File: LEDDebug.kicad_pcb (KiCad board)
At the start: 2 copper layers, 17.5 x 23.9 mm, 34 parts, among them J1 Conn_01x09_Pin

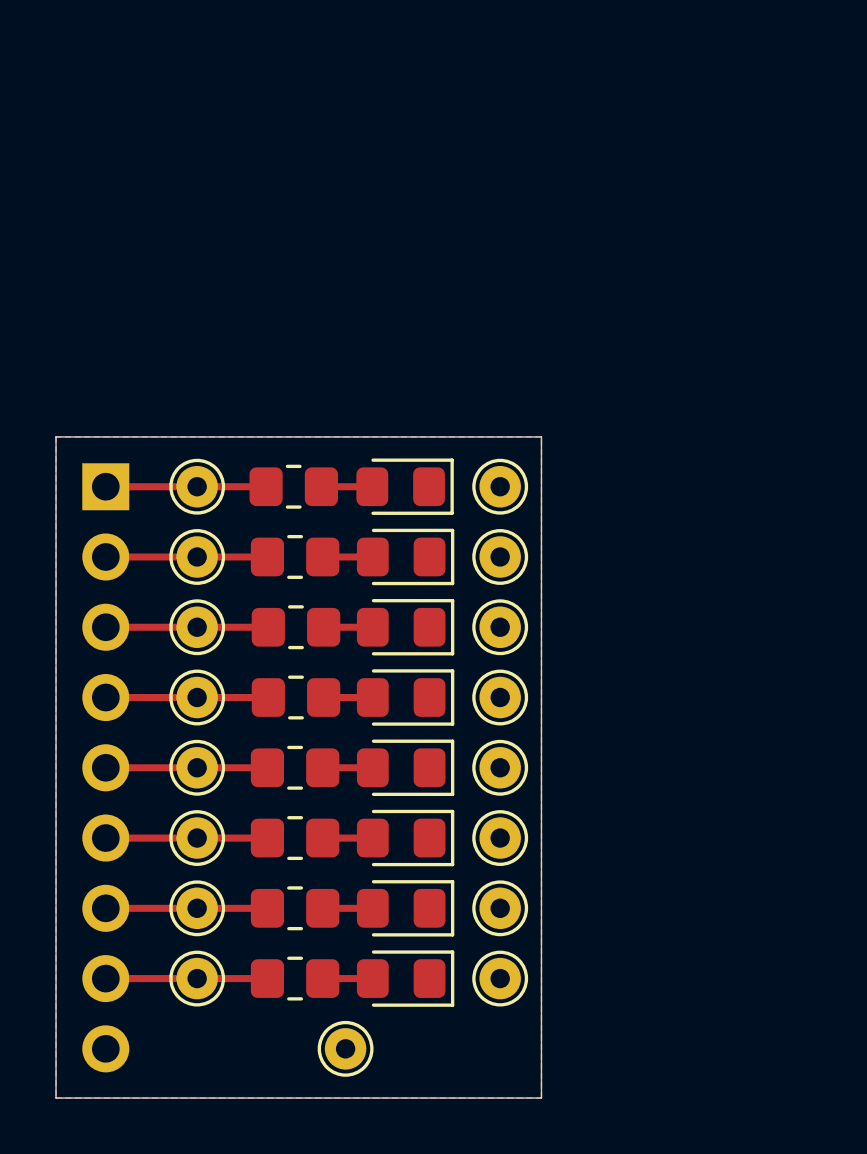
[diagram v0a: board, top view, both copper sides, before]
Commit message: Component sizing and placement update
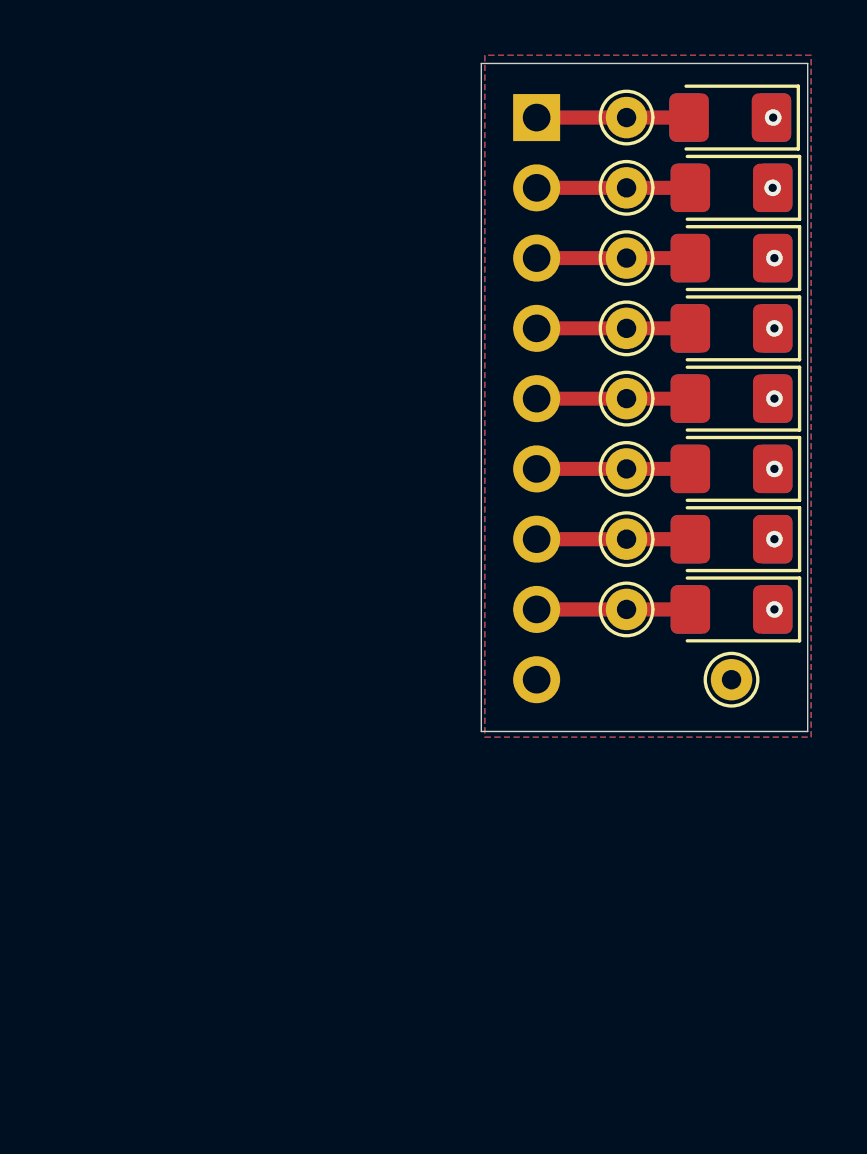
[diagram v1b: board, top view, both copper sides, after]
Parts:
- removed the GND1 at (57.2, 53.6)
- removed GND2, GND3, GND4, GND5, GND6, GND7, GND8: TestPoint, TestPoint:TestPoint_THTPad_D1.5mm_Drill0.7mm
- D1, D2, D3, D4, D5, D6, D7, D8: footprint LED_SMD:LED_0805_2012Metric_Pad1.15x1.40mm_HandSolder -> LED_SMD:LED_1206_3216Metric_Pad1.42x1.75mm_HandSolder
- R1, R2, R3, R4, R5, R6, R7, R8: footprint Resistor_SMD:R_0805_2012Metric_Pad1.20x1.40mm_HandSolder -> Resistor_SMD:R_1206_3216Metric_Pad1.30x1.75mm_HandSolder; moved to B.Cu
- moved R1 20.7 mm to (65.5, 40.2), turned to 0 degrees
- moved R2 20.7 mm to (65.5, 42.8), turned to 0 degrees
- moved R5 20.7 mm to (65.5, 50.4), turned to 0 degrees
- moved R7 20.7 mm to (65.5, 55.5), turned to 0 degrees
- moved R6 20.7 mm to (65.5, 53.0), turned to 0 degrees
- moved R8 20.7 mm to (65.5, 58.0), turned to 0 degrees
- moved R3 20.6 mm to (65.5, 45.3), turned to 0 degrees
- moved R4 20.6 mm to (65.5, 47.9), turned to 0 degrees
- moved J1 20.5 mm to (58.5, 40.2)
- moved TP1 20.5 mm to (61.8, 40.2)
- moved TP2 20.5 mm to (61.8, 42.8)
- moved TP3 20.5 mm to (61.8, 45.3)
- moved TP4 20.5 mm to (61.8, 47.9)
- moved TP5 20.5 mm to (61.8, 50.4)
- moved TP7 20.5 mm to (61.8, 55.5)
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- renumbered GND0 to GND1
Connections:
- D1 pad 1: GND -> Net-(D1-K)
- D1 pad 2: Net-(D1-A) -> TP1
- D2 pad 1: GND -> Net-(D2-K)
- D2 pad 2: Net-(D2-A) -> TP2
- D3 pad 1: GND -> Net-(D3-K)
- D3 pad 2: Net-(D3-A) -> TP3
- D4 pad 1: GND -> Net-(D4-K)
- D4 pad 2: Net-(D4-A) -> TP4
- D5 pad 1: GND -> Net-(D5-K)
- D5 pad 2: Net-(D5-A) -> TP5
- D6 pad 1: GND -> Net-(D6-K)
- D6 pad 2: Net-(D6-A) -> TP6
- D7 pad 1: GND -> Net-(D7-K)
- D7 pad 2: Net-(D7-A) -> TP7
- D8 pad 1: GND -> Net-(D8-K)
- D8 pad 2: Net-(D8-A) -> TP8
- R1 pad 1: Net-(D1-A) -> GND
- R1 pad 2: TP1 -> Net-(D1-K)
- R2 pad 1: Net-(D2-A) -> GND
- R2 pad 2: TP2 -> Net-(D2-K)
- R3 pad 1: Net-(D3-A) -> GND
- R3 pad 2: TP3 -> Net-(D3-K)
- R4 pad 1: Net-(D4-A) -> GND
- R4 pad 2: TP4 -> Net-(D4-K)
- R5 pad 1: Net-(D5-A) -> GND
- R5 pad 2: TP5 -> Net-(D5-K)
- R6 pad 1: Net-(D6-A) -> GND
- R6 pad 2: TP6 -> Net-(D6-K)
- R7 pad 1: Net-(D7-A) -> GND
- R7 pad 2: TP7 -> Net-(D7-K)
- R8 pad 1: Net-(D8-A) -> GND
- R8 pad 2: TP8 -> Net-(D8-K)
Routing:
- net Net-(D1-A): track 1.84 -> 0.00 mm
- net Net-(D8-A): track 1.81 -> 0.00 mm
- net Net-(D7-A): track 1.81 -> 0.00 mm
- net Net-(D6-A): track 1.81 -> 0.00 mm
- net Net-(D5-A): track 1.81 -> 0.00 mm
- net Net-(D2-A): track 1.81 -> 0.00 mm
- net Net-(D4-A): track 1.78 -> 0.00 mm
- net Net-(D3-A): track 1.78 -> 0.00 mm
- net Net-(D8-K): vias 0 -> 1
- net Net-(D7-K): vias 0 -> 1
- net Net-(D6-K): vias 0 -> 1
- net Net-(D5-K): vias 0 -> 1
- net Net-(D4-K): vias 0 -> 1
- net Net-(D3-K): vias 0 -> 1
- net Net-(D2-K): vias 0 -> 1
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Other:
- board size 17.5 x 23.9 mm -> 11.8 x 24.1 mm
